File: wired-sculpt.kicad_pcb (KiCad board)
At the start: 2 copper layers, 40 x 54 mm, 40 parts, among them J1 USB_C_Receptacle, J2 FFC3B07-30-T, J3 AVR-ISP-6 - NOT FITTED, Q1 BSS84AK,215, Q2 2N7002BK,215, SW1 FSMSM, U1 USBLC6-2SC6, U2 LM2776DBVT, U3 AT90USB1286-AUR, Y1 TSX-3225 16.0000MF18X-AC0

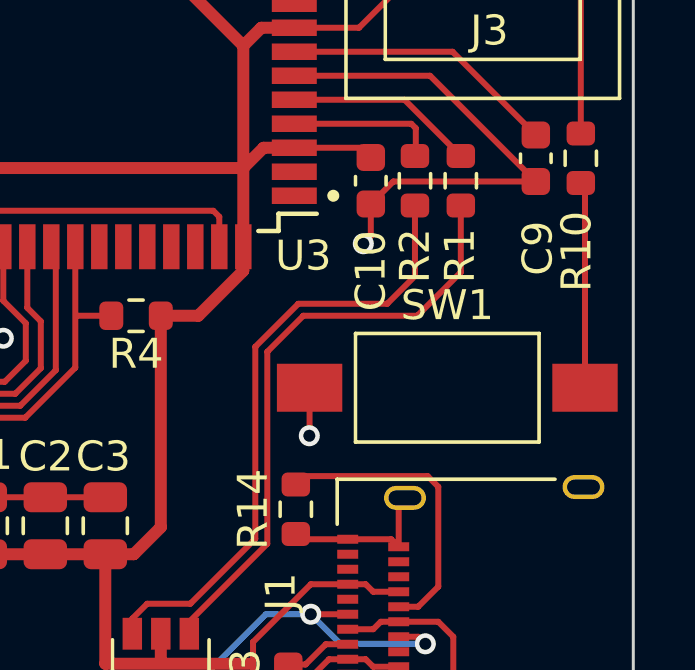
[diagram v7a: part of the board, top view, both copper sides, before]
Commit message: Change reset switch to horizontal
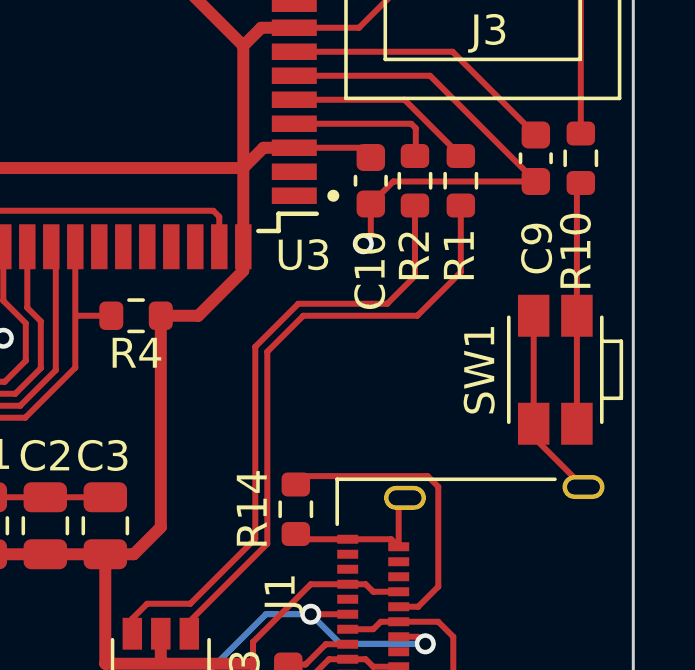
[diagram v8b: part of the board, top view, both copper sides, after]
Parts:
- SW1: value FSMSM -> EVQ-P7A01P; footprint Button_Switch_SMD:SW_SPST_FSMSM -> Button_Switch_SMD:SW_SPST_EVQP7A
- moved SW1 3.65 mm to (157.4, 63.8), turned to 90 degrees
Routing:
- net GND: track 80.9 -> 85.7 mm, vias 12 -> 11
- net Net-(R10-Pad2): track 6.69 -> 8.08 mm
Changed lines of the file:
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@@
     )
   )
-  (footprint "Button_Switch_SMD:SW_SPST_FSMSM" (layer "F.Cu")
-    (at 153.8 64.4)
-    (descr "http://www.te.com/commerce/DocumentDelivery/DDEController?Action=srchrtrv&DocNm=1437566-3&DocType=Customer+Drawing&DocLang=English")
-    (tags "SPST button tactile switch")
-    (property "MPN" "FSMSM")
-    (property "Sheetfile" "wired-sculpt.kicad_sch")
-    (property "Sheetname" "")
-    (attr smd)
-    (fp_text reference "SW1" (at 0 -2.75) (layer "F.SilkS")
-      (effects (font (size 1 1) (thickness 0.15)))
-    )
-    (fp_text value "FSMSM" (at 0 3) (layer "F.Fab")
-      (effects (font (size 1 1) (thickness 0.15)))
-    )
-    (fp_text user "${REFERENCE}" (at 0 -2.6) (layer "F.Fab")
-      (effects (font (size 1 1) (thickness 0.15)))
-    )
-    (fp_line (start 3.06 1.81) (end -3.06 1.81) (layer "F.SilkS") (width 0.12))
-    (fp_line (start 3.06 -1.81) (end 3.06 1.81) (layer "F.SilkS") (width 0.12))
-    (fp_line (start -3.06 1.81) (end -3.06 -1.81) (layer "F.SilkS") (width 0.12))
-    (fp_line (start -3.06 -1.81) (end 3.06 -1.81) (layer "F.SilkS") (width 0.12))
-    (fp_line (start -5.95 2) (end 5.95 2) (layer "F.CrtYd") (width 0.05))
-    (fp_line (start -5.95 -2) (end -5.95 2) (layer "F.CrtYd") (width 0.05))
-    (fp_line (start -5.95 -2) (end 5.95 -2) (layer "F.CrtYd") (width 0.05))
-    (fp_line (start 5.95 -2) (end 5.95 2) (layer "F.CrtYd") (width 0.05))
-    (fp_line (start -3 -1.75) (end -3 1.75) (layer "F.Fab") (width 0.1))
-    (fp_line (start -1.5 0.8) (end 1.5 0.8) (layer "F.Fab") (width 0.1))
-    (fp_line (start -1.75 -1) (end 1.75 -1) (layer "F.Fab") (width 0.1))
-    (fp_line (start 1.75 1) (end -1.75 1) (layer "F.Fab") (width 0.1))
-    (fp_line (start -3 1.75) (end 3 1.75) (layer "F.Fab") (width 0.1))
-    (fp_line (start 3 -1.75) (end 3 1.75) (layer "F.Fab") (width 0.1))
-    (fp_line (start -1.75 1) (end -1.75 -1) (layer "F.Fab") (width 0.1))
-    (fp_line (start -1.5 -0.8) (end -1.5 0.8) (layer "F.Fab") (width 0.1))
-    (fp_line (start 1.75 -1) (end 1.75 1) (layer "F.Fab") (width 0.1))
-    (fp_line (start -1.5 -0.8) (end 1.5 -0.8) (layer "F.Fab") (width 0.1))
-    (fp_line (start 1.5 -0.8) (end 1.5 0.8) (layer "F.Fab") (width 0.1))
-    (fp_line (start -3 -1.75) (end 3 -1.75) (layer "F.Fab") (width 0.1))
-    (pad "1" smd rect locked (at -4.59 0) (size 2.18 1.6) (layers "F.Cu" "F.Paste" "F.Mask")
+  (footprint "Button_Switch_SMD:SW_SPST_EVQP7A" (layer "F.Cu")
+    (at 157.4 63.8 90)
+    (descr "Light Touch Switch,https://industrial.panasonic.com/cdbs/www-data/pdf/ATK0000/ATK0000CE20.pdf")
+    (property "MPN" "EVQ-P7A01P")
+    (property "Sheetfile" "wired-sculpt.kicad_sch")
+    (property "Sheetname" "")
+    (attr smd)
+    (fp_text reference "SW1" (at 0 -2.5 90) (layer "F.SilkS")
+      (effects (font (size 1 1) (thickness 0.15)))
+    )
+    (fp_text value "EVQ-P7A01P" (at 0 3.25 90) (layer "F.Fab")
+      (effects (font (size 1 1) (thickness 0.15)))
+    )
+    (fp_text user "${REFERENCE}" (at 0 -2.5 90) (layer "F.Fab")
+      (effects (font (size 1 1) (thickness 0.15)))
+    )
+    (fp_line (start 0.95 1.55) (end 0.95 2.2) (layer "F.SilkS") (width 0.12))
+    (fp_line (start -1.75 -1.55) (end 1.75 -1.55) (layer "F.SilkS") (width 0.12))
+    (fp_line (start -0.95 2.2) (end -0.95 1.55) (layer "F.SilkS") (width 0.12))
+    (fp_line (start 1.75 1.55) (end -1.75 1.55) (layer "F.SilkS") (width 0.12))
+    (fp_line (start 0.95 2.2) (end -0.95 2.2) (layer "F.SilkS") (width 0.12))
+    (fp_line (start 2.75 1.7) (end 1.1 1.7) (layer "F.CrtYd") (width 0.05))
+    (fp_line (start -1.1 2.35) (end -1.1 1.7) (layer "F.CrtYd") (width 0.05))
+    (fp_line (start -1.1 1.7) (end -2.75 1.7) (layer "F.CrtYd") (width 0.05))
+    (fp_line (start -2.75 1.7) (end -2.75 -1.7) (layer "F.CrtYd") (width 0.05))
+    (fp_line (start 1.1 2.35) (end -1.1 2.35) (layer "F.CrtYd") (width 0.05))
+    (fp_line (start -2.75 -1.7) (end 2.75 -1.7) (layer "F.CrtYd") (width 0.05))
+    (fp_line (start 2.75 -1.7) (end 2.75 1.7) (layer "F.CrtYd") (width 0.05))
+    (fp_line (start 1.1 1.7) (end 1.1 2.35) (layer "F.CrtYd") (width 0.05))
+    (fp_line (start -1.75 -1.45) (end 1.75 -1.45) (layer "F.Fab") (width 0.1))
+    (fp_line (start -0.85 2.1) (end -0.85 1.45) (layer "F.Fab") (width 0.1))
+    (fp_line (start 1.75 1.45) (end -1.75 1.45) (layer "F.Fab") (width 0.1))
+    (fp_line (start -1.75 1.45) (end -1.75 -1.4) (layer "F.Fab") (width 0.1))
+    (fp_line (start 1.75 -1.45) (end 1.75 1.45) (layer "F.Fab") (width 0.1))
+    (fp_line (start -0.85 2.1) (end 0.85 2.1) (layer "F.Fab") (width 0.1))
+    (fp_line (start 0.85 2.1) (end 0.85 1.45) (layer "F.Fab") (width 0.1))
+    (pad "1" smd rect (at 1.8 -0.72 90) (size 1.4 1.05) (layers "F.Cu" "F.Paste" "F.Mask")
       (net 1 "GND") (pinfunction "1") (pintype "passive"))
-    (pad "2" smd rect locked (at 4.59 0) (size 2.18 1.6) (layers "F.Cu" "F.Paste" "F.Mask")
+    (pad "1" smd rect (at -1.8 -0.72 90) (size 1.4 1.05) (layers "F.Cu" "F.Paste" "F.Mask")
+      (net 1 "GND") (pinfunction "1") (pintype "passive"))
+    (pad "2" smd rect (at -1.8 0.72 90) (size 1.4 1.05) (layers "F.Cu" "F.Paste" "F.Mask")
       (net 56 "Net-(R10-Pad2)") (pinfunction "2") (pintype "passive"))
-    (model "${KISYS3DMOD}/Button_Switch_SMD.3dshapes/SW_SPST_FSMSM.wrl"
+    (pad "2" smd rect (at 1.8 0.72 90) (size 1.4 1.05) (layers "F.Cu" "F.Paste" "F.Mask")
+      (net 56 "Net-(R10-Pad2)") (pinfunction "2") (pintype "passive"))
+    (model "${KICAD6_3DMODEL_DIR}/Button_Switch_SMD.3dshapes/SW_SPST_EVQP7A.wrl"
       (offset (xyz 0 0 0))
       (scale (xyz 1 1 1))
@@
   (segment (start 139.65 40.15) (end 139.65 38.9) (width 0.2) (layer "F.Cu") (net 1))
   (segment (start 139.9 40.15) (end 141.05 39) (width 0.2) (layer "F.Cu") (net 1))
-  (segment (start 149.21 65.99) (end 149.2 66) (width 0.2) (layer "F.Cu") (net 1))
   (segment (start 138.2 68.05) (end 137.1 66.95) (width 0.2) (layer "F.Cu") (net 1))
   (segment (start 152 57.525) (end 156.75 57.525) (width 0.2) (layer "F.Cu") (net 1))
   (segment (start 128.3 40) (end 126.5 40) (width 0.2) (layer "F.Cu") (net 1))
+  (segment (start 156.68 62) (end 156.68 65.6) (width 0.2) (layer "F.Cu") (net 1))
   (segment (start 138.2 62.325) (end 138.2 59.7) (width 0.2) (layer "F.Cu") (net 1))
   (segment (start 140 40.15) (end 141.7 41.85) (width 0.2) (layer "F.Cu") (net 1))
@@
   (segment (start 144.72548 40.99952) (end 144.72548 42.217263) (width 0.2) (layer "F.Cu") (net 1))
   (segment (start 145.5 40.225) (end 144.72548 40.99952) (width 0.2) (layer "F.Cu") (net 1))
+  (segment (start 156.68 66.05) (end 158.34 67.71) (width 0.2) (layer "F.Cu") (net 1))
   (segment (start 146 58.5) (end 146.2 58.7) (width 0.2) (layer "F.Cu") (net 1))
   (segment (start 143.779999 39.779999) (end 143.779999 40.225) (width 0.2) (layer "F.Cu") (net 1))
   (segment (start 143 39) (end 143.779999 39.779999) (width 0.2) (layer "F.Cu") (net 1))
+  (segment (start 156.68 65.6) (end 156.68 66.05) (width 0.2) (layer "F.Cu") (net 1))
   (segment (start 138.2 58.55) (end 138.25 58.5) (width 0.2) (layer "F.Cu") (net 1))
   (segment (start 144.25 75.45) (end 145 76.2) (width 0.2) (layer "F.Cu") (net 1))
@@
   (segment (start 148.825 74.95) (end 150.48 74.95) (width 0.2) (layer "F.Cu") (net 1))
   (segment (start 144.25 74.8) (end 144.25 75.45) (width 0.2) (layer "F.Cu") (net 1))
-  (segment (start 149.21 64.4) (end 149.21 65.99) (width 0.2) (layer "F.Cu") (net 1))
   (segment (start 147.5 37) (end 147.475 36.975) (width 0.2) (layer "F.Cu") (net 1))
   (segment (start 148.5 75.275) (end 148.825 74.95) (width 0.2) (layer "F.Cu") (net 1))
@@
   (via (at 123.01 37.01) (size 0.7) (drill 0.4) (layers "F.Cu" "B.Cu") (net 1))
   (via (at 139 62.75) (size 0.7) (drill 0.4) (layers "F.Cu" "B.Cu") (net 1))
-  (via (at 149.2 66) (size 0.7) (drill 0.4) (layers "F.Cu" "B.Cu") (net 1))
   (via (at 137.1 66.95) (size 0.7) (drill 0.4) (layers "F.Cu" "B.Cu") (net 1))
   (via (at 151 59.6) (size 0.7) (drill 0.4) (layers "F.Cu" "B.Cu") (net 1))
@@
   (segment (start 134.349511 58.574511) (end 134.349511 54.349511) (width 0.2) (layer "F.Cu") (net 55))
   (segment (start 132.499022 60.425) (end 134.349511 58.574511) (width 0.2) (layer "F.Cu") (net 55))
-  (segment (start 158.39 64.4) (end 158.39 57.715) (width 0.2) (layer "F.Cu") (net 56))
+  (segment (start 158.12 57.705) (end 158.25 57.575) (width 0.2) (layer "F.Cu") (net 56))
+  (segment (start 158.12 65.6) (end 158.12 62) (width 0.2) (layer "F.Cu") (net 56))
+  (segment (start 158.12 62) (end 158.12 57.705) (width 0.2) (layer "F.Cu") (net 56))
   (segment (start 130.75 41.075) (end 128.375 41.075) (width 0.2) (layer "F.Cu") (net 71))
   (segment (start 128.3 42) (end 131.546096 42) (width 0.2) (layer "F.Cu") (net 72))
